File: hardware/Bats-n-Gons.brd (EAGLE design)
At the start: 160 x 100 mm, 4 parts, among them X4 32.768

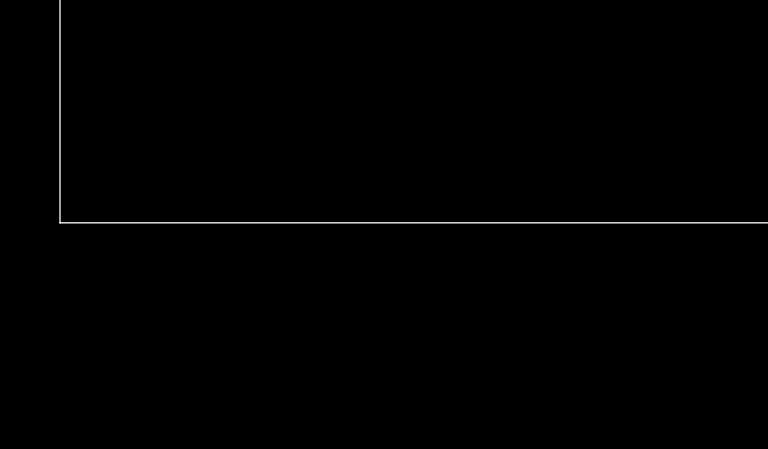
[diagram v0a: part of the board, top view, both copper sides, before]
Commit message: replaced spaces in file names with dashes added local library for components
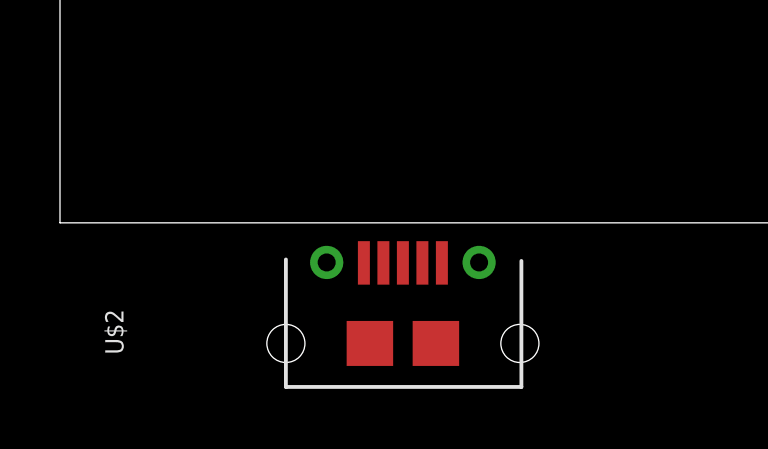
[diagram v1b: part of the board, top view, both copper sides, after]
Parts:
- added U$2: (no value), SophiEaglev9:USB_MICRO_LEGS_2
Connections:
- new net VBUS: U$2.VBUS
- net GND: now also U$2.GND
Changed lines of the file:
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@@
 <layer number="132" name="bAdjust" color="7" fill="1" visible="no" active="no"/>
 <layer number="133" name="bottom_silk" color="7" fill="1" visible="yes" active="yes"/>
+<layer number="134" name="silk_top" color="7" fill="1" visible="no" active="no"/>
+<layer number="135" name="silk_bottom" color="7" fill="1" visible="no" active="no"/>
+<layer number="136" name="silktop" color="7" fill="1" visible="yes" active="yes"/>
+<layer number="137" name="silkbottom" color="7" fill="1" visible="yes" active="yes"/>
 <layer number="144" name="Drill_legend" color="7" fill="1" visible="yes" active="yes"/>
+<layer number="145" name="DrillLegend_01-16" color="7" fill="1" visible="yes" active="yes"/>
+<layer number="146" name="DrillLegend_01-20" color="7" fill="1" visible="yes" active="yes"/>
 <layer number="150" name="Notes" color="7" fill="1" visible="no" active="no"/>
 <layer number="151" name="HeatSink" color="7" fill="1" visible="no" active="yes"/>
@@
 <layer number="154" name="FabDoc2" color="2" fill="1" visible="no" active="no"/>
 <layer number="155" name="FabDoc3" color="7" fill="15" visible="no" active="no"/>
+<layer number="166" name="AntennaArea" color="7" fill="1" visible="yes" active="yes"/>
+<layer number="168" name="4mmHeightArea" color="7" fill="1" visible="yes" active="yes"/>
 <layer number="199" name="Contour" color="7" fill="1" visible="no" active="no"/>
 <layer number="200" name="200bmp" color="1" fill="10" visible="no" active="no"/>
@@
 <attribute name="VALUE" x="54.55" y="64.7" size="1.016" layer="27" font="vector"/>
 </element>
+<element name="U$2" library="SophiEaglev9" package="USB_MICRO_LEGS_2" value="" x="6.35" y="-5.08" smashed="yes">
+<attribute name="NAME" x="2.116934375" y="-4.389778125" size="0.6096" layer="25" font="vector" ratio="20" rot="R90"/>
+<attribute name="VALUE" x="18.929" y="-5.43" size="0.6096" layer="27" font="vector" ratio="20" rot="R90" align="top-left"/>
+</element>
 </elements>
 <signals>
@@
 <contactref element="C5" pad="2"/>
 <contactref element="C7" pad="2"/>
-<wire x1="47.84" y1="59.69" x2="47.84" y2="50.8" width="0" layer="19" extent="1-1"/>
+<contactref element="U$2" pad="GND"/>
+<wire x1="47.84" y1="50.8" x2="47.84" y2="59.69" width="0" layer="19" extent="1-1"/>
+<wire x1="12.73" y1="-1.335" x2="47.84" y2="50.8" width="0" layer="19" extent="1-1"/>
 </signal>
 <signal name="AREF" class="4">
@@
 <contactref element="U$1" pad="122"/>
 </signal>
+<signal name="VBUS">
+<contactref element="U$2" pad="VBUS"/>
+</signal>
 </signals>

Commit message: continued work on prototype board design
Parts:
- added C1, C2: (no value), yapo:C0603
- added IC1: (no value), yapo:SOT-223
- added J1: (no value), yapo:HEADER_4PIN
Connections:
- removed net VBUS: U$2.VBUS
- new net +3.3V: C2.P$2, IC1.2, IC1.4
- new net +5V: C1.P$2, IC1.3, J1.1, U$2.VBUS
- net D+: now also U$2.D+
- net D-: now also U$2.D-
- net GND: now also C1.P$1, C2.P$1, IC1.1, J1.4
- net UART1_RX: now also J1.2
- net UART1_TX: now also J1.3
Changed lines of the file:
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@@
 <attribute name="VALUE" x="18.929" y="-5.43" size="0.6096" layer="27" font="vector" ratio="20" rot="R90" align="top-left"/>
+</element>
+<element name="IC1" library="yapo" package="SOT-223" value="" x="3.81" y="-11.43" smashed="yes">
+<attribute name="NAME" x="8.11" y="-8.83" size="1.27" layer="25"/>
+<attribute name="VALUE" x="8.11" y="-10.63" size="1.27" layer="27"/>
+</element>
+<element name="C1" library="yapo" package="C0603" value="" x="2.54" y="-19.05" smashed="yes">
+<attribute name="NAME" x="6.35" y="-17.78" size="1.27" layer="25"/>
+<attribute name="VALUE" x="6.35" y="-20.32" size="1.27" layer="27"/>
+</element>
+<element name="C2" library="yapo" package="C0603" value="" x="2.54" y="-24.13" smashed="yes">
+<attribute name="NAME" x="6.35" y="-22.86" size="1.27" layer="25"/>
+<attribute name="VALUE" x="6.35" y="-25.4" size="1.27" layer="27"/>
+</element>
+<element name="J1" library="yapo" package="HEADER_4PIN" value="" x="6.35" y="-33.02" smashed="yes">
+<attribute name="NAME" x="1.27" y="-27.94" size="1.27" layer="25"/>
+<attribute name="VALUE" x="1.27" y="-30.48" size="1.27" layer="27"/>
 </element>
 </elements>
@@
 <contactref element="C7" pad="2"/>
 <contactref element="U$2" pad="GND"/>
+<contactref element="C1" pad="P$1"/>
+<contactref element="IC1" pad="1"/>
+<contactref element="C2" pad="P$1"/>
+<contactref element="J1" pad="4"/>
 <wire x1="47.84" y1="50.8" x2="47.84" y2="59.69" width="0" layer="19" extent="1-1"/>
 <wire x1="12.73" y1="-1.335" x2="47.84" y2="50.8" width="0" layer="19" extent="1-1"/>
+<wire x1="1.51" y1="-14.48" x2="12.73" y2="-1.335" width="0" layer="19" extent="1-1"/>
+<wire x1="1.79" y1="-19.05" x2="1.51" y2="-14.48" width="0" layer="19" extent="1-1"/>
+<wire x1="1.79" y1="-24.13" x2="1.79" y2="-19.05" width="0" layer="19" extent="1-1"/>
+<wire x1="10.16" y1="-33.02" x2="1.79" y2="-24.13" width="0" layer="19" extent="1-1"/>
 </signal>
 <signal name="AREF" class="4">
@@
 <signal name="SCK">
 <contactref element="U$1" pad="48"/>
-</signal>
-<signal name="D-" class="1">
-<contactref element="U$1" pad="94"/>
-</signal>
-<signal name="D+" class="1">
-<contactref element="U$1" pad="95"/>
 </signal>
 <signal name="MISO">
@@
 <signal name="UART1_TX">
 <contactref element="U$1" pad="41"/>
+<contactref element="J1" pad="3"/>
+<wire x1="7.62" y1="-33.02" x2="69.83" y2="43.99" width="0" layer="19" extent="1-1"/>
 </signal>
 <signal name="UART1_RX">
 <contactref element="U$1" pad="42"/>
+<contactref element="J1" pad="2"/>
+<wire x1="5.08" y1="-33.02" x2="69.83" y2="44.39" width="0" layer="19" extent="1-1"/>
 </signal>
 <signal name="UART2_RX">
@@
 <contactref element="U$1" pad="122"/>
 </signal>
-<signal name="VBUS">
+<signal name="D-">
+<contactref element="U$1" pad="94"/>
+<contactref element="U$2" pad="D-"/>
+<wire x1="10.78" y1="-1.335" x2="56.83" y2="54.59" width="0" layer="19" extent="1-1"/>
+</signal>
+<signal name="D+">
+<contactref element="U$1" pad="95"/>
+<contactref element="U$2" pad="D+"/>
+<wire x1="11.43" y1="-1.335" x2="56.43" y2="54.59" width="0" layer="19" extent="1-1"/>
+</signal>
+<signal name="+3.3V">
+<contactref element="C2" pad="P$2"/>
+<contactref element="IC1" pad="2"/>
+<contactref element="IC1" pad="4"/>
+<wire x1="3.81" y1="-14.48" x2="3.29" y2="-24.13" width="0" layer="19" extent="1-1"/>
+<wire x1="3.81" y1="-8.38" x2="3.81" y2="-14.48" width="0" layer="19" extent="1-1"/>
+</signal>
+<signal name="+5V">
 <contactref element="U$2" pad="VBUS"/>
+<contactref element="IC1" pad="3"/>
+<contactref element="C1" pad="P$2"/>
+<contactref element="J1" pad="1"/>
+<wire x1="3.29" y1="-19.05" x2="2.54" y2="-33.02" width="0" layer="19" extent="1-1"/>
+<wire x1="6.11" y1="-14.48" x2="3.29" y2="-19.05" width="0" layer="19" extent="1-1"/>
+<wire x1="10.13" y1="-1.335" x2="6.11" y2="-14.48" width="0" layer="19" extent="1-1"/>
 </signal>
 </signals>

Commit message: checkpoint
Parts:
- moved J1 97.4 mm to (48.9, 54.6), turned to 180 degrees
- moved X4 61.0 mm to (37.5, 5.71), turned to 180 degrees
- moved U$2 59.0 mm to (43.1, 41.1), turned to 180 degrees
- moved C5 54.8 mm to (34.3, 6.35), turned to 90 degrees
- moved C2 52.9 mm to (17.1, 26.7), turned to 90 degrees
- moved C1 47.7 mm to (10.8, 27.9), turned to 270 degrees
- moved IC1 47.6 mm to (17.1, 34.3)
- moved C7 44.9 mm to (40.6, 6.35), turned to 90 degrees
- moved U$1 33.5 mm to (43.8, 19.1)
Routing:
- net D-: track 0.00 -> 10.9 mm
- net D+: track 0.00 -> 10.8 mm
- net N$9: track 0.00 -> 8.42 mm
- net N$12: track 0.00 -> 8.13 mm
- added copper zone on layer 1, net GND
- added copper zone on layer 16, net GND
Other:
- board size 160 x 100 mm -> 71.7 x 65.1 mm

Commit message: checkpoint
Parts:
- added C10: NOPOP, bats-n-gons:C0603
- added C11: 100n, bats-n-gons:C0603
- added C12, C13, C14, C15, C16, C17, C18, C19, C20, C21, C22, C3, C4, C8: (no value), bats-n-gons:C0603
- added C6: 1u, bats-n-gons:C0603
- added C9: 10u, bats-n-gons:1206
- added D13_LED, PWR_LED, RX_LED, TX_LED: (no value), bats-n-gons:LED_0603
- added IC2: IS31AP4991, bats-n-gons:SOIC8
- added R1, R5, R6, R7, R8: (no value), bats-n-gons:R0603
- added R2, R3: 20k, bats-n-gons:R0603
- added R4: 100, bats-n-gons:R0603
- added SPK+, SPK-: PAD100MIL, bats-n-gons:PAD_100MIL
- added U$23: SMD_SWITCH, bats-n-gons:SMD_SWITCH
- C1, C2: value (none) -> 1u
- moved X4 34.6 mm to (61.6, 30.5), turned to 270 degrees
- moved C5 33.9 mm to (61.0, 27.3), turned to 180 degrees
- moved C7 33.7 mm to (64.1, 30.5), turned to 270 degrees
- moved C2 30.1 mm to (34.3, 51.4), turned to 180 degrees
- moved C1 26.6 mm to (27.9, 48.3), turned to 90 degrees
- moved IC1 19.9 mm to (33.0, 46.4), turned to 180 degrees
- moved U$1 18.3 mm to (48.3, 36.8), turned to 90 degrees
- moved U$2 17.6 mm to (26.2, 36.1), turned to 270 degrees
- moved J1 2.01 mm to (50.8, 55.2), turned to 0 degrees
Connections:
- new net N$1: C6.P$1, IC2.1, IC2.5
- new net N$10: D13_LED.A, R6.P$2
- new net N$11: R7.P$2, TX_LED.A
- new net N$13: R8.P$2, RX_LED.A
- new net N$2: C10.P$2, IC2.2, R2.P$2, SPK-.P$1
- new net N$3: C10.P$1, IC2.3, R2.P$1, R3.P$2
- new net N$4: C11.P$2, R3.P$1
- new net N$5: IC2.6, SPK+.P$1
- new net N$6: C22.P$2, R1.P$2, U$1.114, U$23.P$3, U$23.P$4
- new net N$7: J1.3, R4.P$2
- new net N$8: PWR_LED.A, R5.P$2
- net +3.3V: now also C12.P$2, C13.P$2, C14.P$2, C15.P$2, C16.P$2, C17.P$2, C18.P$2, C19.P$2, C20.P$2, C21.P$2, C3.P$2, C4.P$2, C8.P$2, C9.P$1, IC2.8, R1.P$1, R5.P$1, U$1.107, U$1.118, U$1.15, U$1.26, U$1.32, U$1.37, U$1.46, U$1.54, U$1.6, U$1.65, U$1.79, U$1.91, U$1.97
- net A0: now also C11.P$1
- net D13: now also R6.P$1
- net D2: now also IC2.7
- net GND: now also C12.P$1, C13.P$1, C14.P$1, C15.P$1, C16.P$1, C17.P$1, C18.P$1, C19.P$1, C20.P$1, C21.P$1, C22.P$1, C3.P$1, C4.P$1, C6.P$2, C8.P$1, C9.P$2, D13_LED.C, IC2.4, PWR_LED.C, RX_LED.C, TX_LED.C, U$1.106, U$1.116, U$1.14, U$1.25, U$1.31, U$1.38, U$1.45, U$1.5, U$1.53, U$1.64, U$1.78, U$1.90, U$1.96, U$23.P$1, U$23.P$2
- net RXLED: now also R8.P$1
- net TXLED: now also R7.P$1
- net UART1_TX: now also R4.P$1; no longer J1.3
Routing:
- net +5V: track 0.00 -> 48.9 mm
- net +3.3V: track 0.00 -> 45.1 mm, vias 0 -> 16
- net D2: track 0.00 -> 38.9 mm, vias 0 -> 2
- net N$6: track 0.00 -> 24.7 mm
- net N$2: track 0.00 -> 21.8 mm, vias 0 -> 4
- net A0: track 0.00 -> 17.2 mm
- net N$5: track 0.00 -> 13.5 mm, vias 0 -> 4
- net D13: track 0.00 -> 12.3 mm
- net N$3: track 0.00 -> 12.0 mm
- net UART1_RX: track 0.00 -> 11.4 mm
- net RXLED: track 0.00 -> 10.5 mm
- net N$1: track 0.00 -> 9.58 mm
- net TXLED: track 0.00 -> 9.23 mm
- net UART1_TX: track 0.00 -> 6.62 mm
- net N$8: track 0.00 -> 3.19 mm
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- added copper zone on layer 1, net +3.3V
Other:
- board size 71.7 x 65.1 mm -> 85.7 x 65.1 mm
- board text added: "+5"
- board text added: "GND"
- board text added: "NETWORK"
- board text added: "RX"
- board text added: "TX"
- board text added: "place me"

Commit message: wheeeee
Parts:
- added D1, D2: DIFFUSE, SparkFun-LED:LED-RGB-THRU
- added D13_LED1, PWR_LED1: (no value), bats-n-gons:LED_0603
- added J2: (no value), SparkFun-Connectors:1X03
- added R9: 100, bats-n-gons:R0603
- moved C13 30.9 mm to (32.9, 24.0)
- moved C17 30.6 mm to (32.9, 26.4)
- moved C21 26.6 mm to (69.2, 35.7), turned to 180 degrees
- moved PWR_LED 21.2 mm to (20.2, 54.7)
- moved R5 20.6 mm to (18.2, 50.8)
- moved C11 5.39 mm to (73.7, 33.0)
- moved R3 4.89 mm to (78.0, 26.9)
- moved C7 3.24 mm to (61.2, 31.9), turned to 0 degrees
- moved C5 2.30 mm to (61.2, 25.0), turned to 0 degrees
- moved X4 2.05 mm to (61.3, 28.4)
- moved C19 0.76 mm to (61.0, 43.1)
- moved C8 0.53 mm to (61.0, 40.6)
- moved C16 0.51 mm to (61.0, 36.2)
- moved C20 0.51 mm to (61.0, 33.7)
- renumbered IC1 to U3, IC2 to U2, R4 to R10, U$1 to U1, U$2 to USB, U$23 to SW1
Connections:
- new net N$14: J1.2, R9.P$2
- net +5V: now also J2.3
- net UART1_RX: now also R9.P$1; no longer J1.2
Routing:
- net GND: track 0.00 -> 178.8 mm, vias 20 -> 22
- net +3.3V: track 45.1 -> 105.8 mm, vias 16 -> 15
- net D2: track 38.9 -> 0.00 mm, vias 2 -> 0
- net N$4: track 2.34 -> 8.91 mm
- net UART1_RX: track 11.4 -> 6.84 mm
- net N$3: track 12.0 -> 7.95 mm
- net N$14: track 0.00 -> 3.21 mm
- net N$8: track 3.19 -> 0.00 mm
- net D13: track 12.3 -> 14.3 mm
- net RXLED: track 10.5 -> 12.3 mm
- net N$12: track 8.87 -> 7.59 mm
- net A0: track 17.2 -> 18.1 mm
- net TXLED: track 9.23 -> 10.0 mm
- net N$9: track 8.42 -> 9.15 mm
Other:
- board text removed: "NETWORK"
- board text removed: "place me"

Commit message: maybe good enough for 0.0
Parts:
- removed D13_LED1, PWR_LED1: (no value), bats-n-gons:LED_0603
- removed J2: (no value), SparkFun-Connectors:1X03
- added C23: 0.1u, bats-n-gons:C0603
- added C24: (no value), bats-n-gons:C0603
- added L1: 10u, bats-n-gons:L24X24
- added PAD_TOUCH, PAD_TOUCH1: PAD, bats-n-gons:PAD-ROUND-100MIL-MASK
- added U$1: HEADER_3PIN, bats-n-gons:HEADER_3PIN
- added U$33, U$34: PADROUND-50MIL, bats-n-gons:PAD-ROUND-50MIL
- C21: value (none) -> 10u
- D1, D2: value DIFFUSE -> (none); device SparkFun-LED:LED-RGB-THRU -> bats-n-gons:LED-RGB-THRU
- moved C21 46.7 mm to (26.2, 17.5), turned to 270 degrees
- moved D2 35.1 mm to (11.2, 5.84)
- moved C10 27.6 mm to (51.7, 21.1)
- moved R2 27.6 mm to (51.7, 23.6)
- moved U2 27.6 mm to (51.7, 29.3)
- moved C11 27.6 mm to (47.2, 24.9)
- moved C6 27.6 mm to (56.1, 31.9)
- moved C9 27.6 mm to (47.2, 29.3)
- moved R3 27.6 mm to (51.6, 18.8)
- moved SPK+ 27.6 mm to (57.4, 37.0)
- moved SPK- 27.6 mm to (57.4, 23.6)
- moved USB 27.4 mm to (0.00, 27.9)
- moved PWR_LED 26.7 mm to (5.21, 32.6), turned to 270 degrees
- moved C15 24.3 mm to (23.2, 17.3)
- moved X4 23.8 mm to (39.0, 20.3)
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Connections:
- net N$6 renamed !RESET!
- new net N$15: U$1.3, USB.VBUS
- new net N$16: J1.1, U$1.1
- new net N$17: D1.4, D2.1
- new net N$18: C21.P$2, C23.P$2, L1.1, U1.115
- new net N$19: L1.2, U1.117
- net +3.3V: now also C24.P$2, U$33.P$1; no longer C21.P$2
- net +5V: now also D1.2, D2.2, U$1.2, U$34.P$1; no longer J1.1, J2.3, USB.VBUS
- net A1: now also PAD_TOUCH1.P$1
- net A2: now also PAD_TOUCH.P$1
- net D2: no longer U2.7
- net D46: now also U2.7
- net GND: now also C23.P$1, C24.P$1, D1.3, D2.3
- net NEOPIX: now also D1.1
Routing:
- net GND: track 178.8 -> 1.43 mm, vias 22 -> 61
- net N$15: track 0.00 -> 31.3 mm
- net +3.3V: track 105.8 -> 135.5 mm, vias 15 -> 21
- net N$17: track 0.00 -> 20.8 mm
- net A2: track 0.00 -> 20.8 mm
- net D46: track 0.00 -> 19.9 mm
- net NEOPIX: track 0.00 -> 18.7 mm
- net N$16: track 0.00 -> 17.0 mm
- net A1: track 0.00 -> 8.17 mm
- net +5V: track 48.9 -> 56.8 mm, vias 0 -> 1
- net N$18: track 0.00 -> 6.86 mm
- net A0: track 18.1 -> 13.0 mm
- net D+: track 10.8 -> 15.6 mm
- net D-: track 10.9 -> 15.8 mm
- net N$19: track 0.00 -> 3.76 mm
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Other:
- board size 85.7 x 65.1 mm -> 59.4 x 53.3 mm
- board text added: "+3.3"
- board text added: "3/7/2020"
- board text added: "Bats n Gons 0.0"
- board text added: "CAVE"
- board text added: "D1"
- board text added: "D13"
- board text added: "D2"
- board text added: "Kravitz/Yapo"
- board text added: "POWER"
- board text added: "SUPPLY"
- board text added: "TOUCH"
- board text added: "USB"
